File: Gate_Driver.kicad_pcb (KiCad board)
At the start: 2 copper layers, 110.3 x 47.3 mm, 25 parts, among them J1 171857-0002, J2 171857-0002

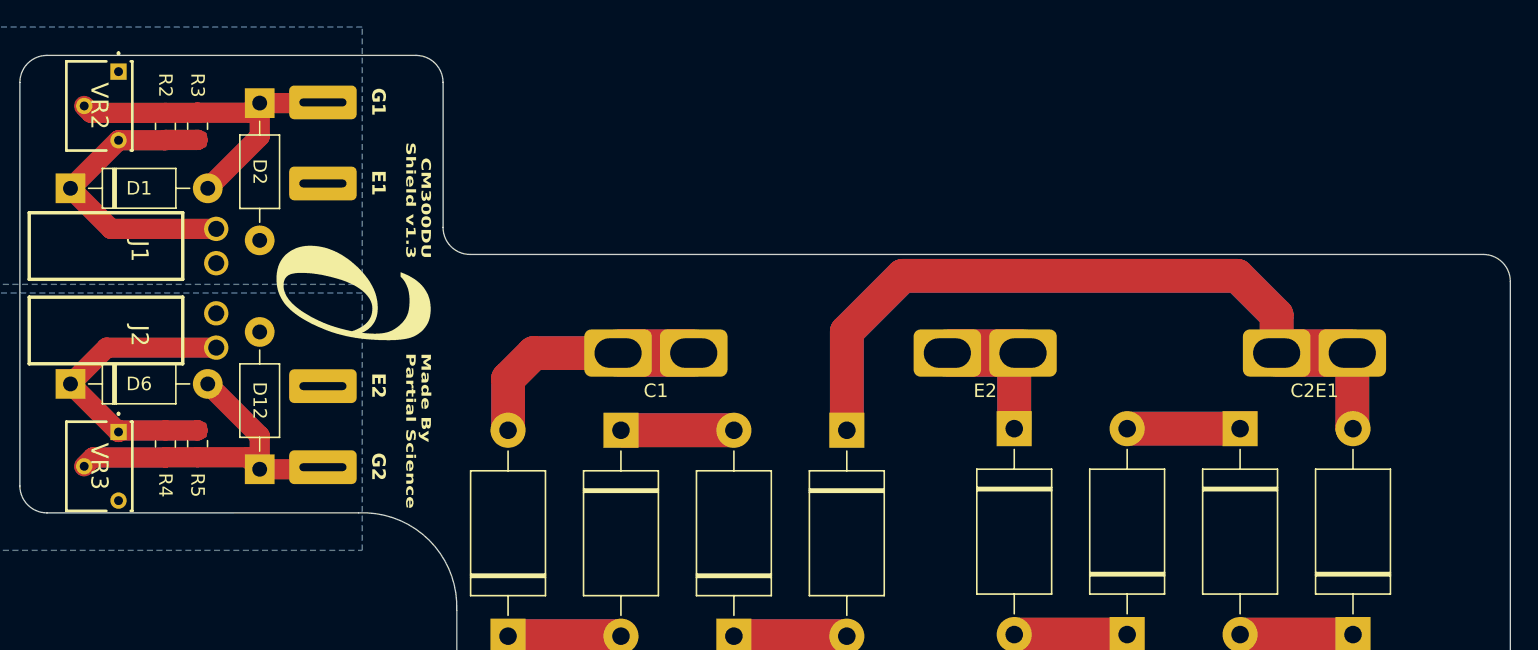
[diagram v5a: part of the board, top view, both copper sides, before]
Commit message: Route longer C1-E1 trace as a filled zone
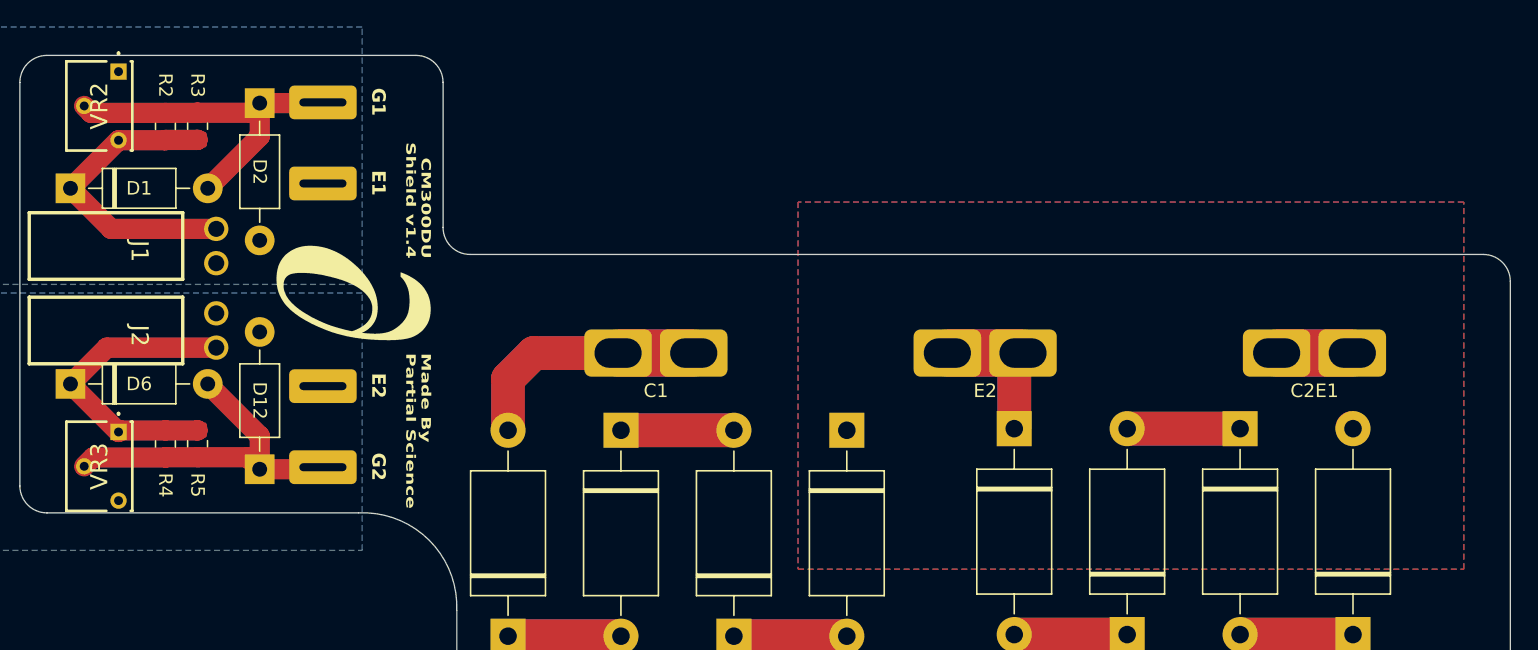
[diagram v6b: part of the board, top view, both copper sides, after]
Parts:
- D10, D11, D3, D4, D5, D7, D8, D9: value 1.5KExxCA -> 1.5KE220CA
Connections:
- Q1 pad 1.5: Net-(D12-K) -> (no net)
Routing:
- net Net-(C2E1-Pin_1): track 112.1 -> 11.3 mm
- added copper zone on B.Cu, net Net-(C2E1-Pin_1)
- added copper zone on F.Cu, net Net-(C2E1-Pin_1)
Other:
- board text added: "CM300DU Shield v1.4"
- board text removed: "CM300DU Shield v1.3"
